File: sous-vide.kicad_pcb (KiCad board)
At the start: 2 copper layers, 100 x 70 mm, 31 parts, among them J1 Heater, J2 Power, J3 Conn_01x02, J4 Jumper, J5 Jumper, Q1 2N3904, SW1 SW_Push_Dual, SW2 SW_Push_Dual, U1 G5LE, U2 RAC01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

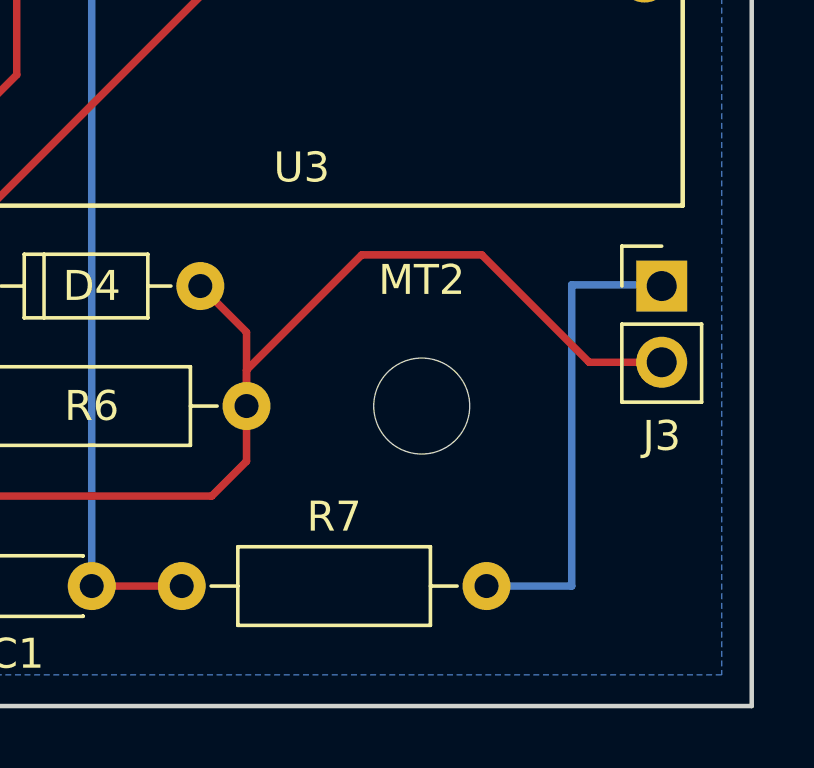
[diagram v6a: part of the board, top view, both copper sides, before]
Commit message: new schematic using NC7SB analog multiplexer
 - requires surface mount :(
 - re-annotated everything so routing will be very annoying

Also, I was testing to see why/how relay load affected analog readings
and I discovered a few odd things:

 - D4/GPIO2/Blue_LED does not light up. low voltage?
 - using a transistor on *just* the pot (instead of GPIO directly)
 seemed to remove effect of relay
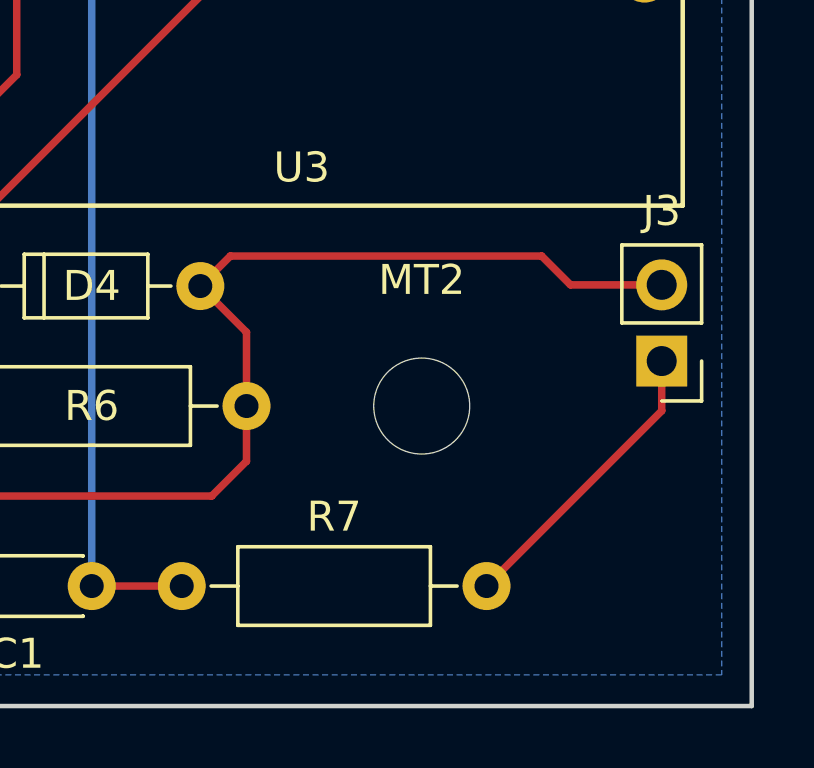
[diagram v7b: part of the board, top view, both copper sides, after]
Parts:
- moved J3 2.50 mm to (203.0, 93.5), turned to 180 degrees
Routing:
- net Net-(J3-Pad1): track 15.9 -> 9.98 mm
- net Net-(C1-Pad2): track 37.6 -> 35.7 mm
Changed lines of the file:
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@@
     (thickness 1.6)
     (drawings 95)
-    (tracks 142)
+    (tracks 139)
     (zones 0)
     (modules 31)
@@
   )
   (module Pin_Headers:Pin_Header_Straight_1x02_Pitch2.54mm (layer F.Cu)
-    (at 203 91)
+    (at 203 93.5 180)
     (descr "Through hole straight pin header, 1x02, 2.54mm pitch, single row")
     (tags "Through hole pin header THT 1x02 2.54mm single row")
-    (fp_text reference J3 (at 0 5) (layer F.SilkS)
-      (effects (font (size 1 1) (thickness 0.15)))
-    )
-    (fp_text value Conn_01x02 (at 0 4.87) (layer F.Fab)
+    (fp_text reference J3 (at 0 5 180) (layer F.SilkS)
+      (effects (font (size 1 1) (thickness 0.15)))
+    )
+    (fp_text value Conn_01x02 (at 0 4.87 180) (layer F.Fab)
       (effects (font (size 1 1) (thickness 0.15)))
     )
@@
     (fp_line (start 1.8 4.35) (end 1.8 -1.8) (layer F.CrtYd) (width 0.05))
     (fp_line (start 1.8 -1.8) (end -1.8 -1.8) (layer F.CrtYd) (width 0.05))
-    (fp_text user %R (at 0 1.27 90) (layer F.Fab)
-      (effects (font (size 1 1) (thickness 0.15)))
-    )
-    (pad 1 thru_hole rect (at 0 0) (size 1.7 1.7) (drill 1) (layers *.Cu *.Mask)
+    (fp_text user %R (at 0 1.27 270) (layer F.Fab)
+      (effects (font (size 1 1) (thickness 0.15)))
+    )
+    (pad 1 thru_hole rect (at 0 0 180) (size 1.7 1.7) (drill 1) (layers *.Cu *.Mask)
       (net 33 "Net-(J3-Pad1)"))
-    (pad 2 thru_hole oval (at 0 2.54) (size 1.7 1.7) (drill 1) (layers *.Cu *.Mask)
+    (pad 2 thru_hole oval (at 0 2.54 180) (size 1.7 1.7) (drill 1) (layers *.Cu *.Mask)
       (net 32 "Net-(C1-Pad2)"))
     (model ${KISYS3DMOD}/Pin_Headers.3dshapes/Pin_Header_Straight_1x02_Pitch2.54mm.wrl
@@
   (segment (start 121.5 39.38) (end 117.8575 39.38) (width 2.5) (layer B.Cu) (net 23))
   (segment (start 136.76 39.38) (end 121.5 39.38) (width 2.5) (layer B.Cu) (net 23))
-  (segment (start 203 93.54) (end 200.58 93.54) (width 0.25) (layer F.Cu) (net 32))
-  (segment (start 189.16 93.8) (end 189.16 95) (width 0.25) (layer F.Cu) (net 32))
-  (segment (start 193 89.96) (end 189.16 93.8) (width 0.25) (layer F.Cu) (net 32))
-  (segment (start 197 89.96) (end 193 89.96) (width 0.25) (layer F.Cu) (net 32))
-  (segment (start 200.58 93.54) (end 197 89.96) (width 0.25) (layer F.Cu) (net 32))
+  (segment (start 203 90.96) (end 199.96 90.96) (width 0.25) (layer F.Cu) (net 32))
+  (segment (start 188.62 90) (end 187.62 91) (width 0.25) (layer F.Cu) (net 32))
+  (segment (start 199 90) (end 188.62 90) (width 0.25) (layer F.Cu) (net 32))
+  (segment (start 199.96 90.96) (end 199 90) (width 0.25) (layer F.Cu) (net 32))
   (segment (start 189.16 95) (end 189.16 92.54) (width 0.25) (layer F.Cu) (net 32) (status 10))
   (segment (start 189.16 92.54) (end 187.62 91) (width 0.25) (layer F.Cu) (net 32) (status 20))
@@
   (segment (start 188 98) (end 180 98) (width 0.25) (layer F.Cu) (net 32))
   (segment (start 189.16 96.84) (end 188 98) (width 0.25) (layer F.Cu) (net 32))
-  (segment (start 200 90.96) (end 202.96 90.96) (width 0.25) (layer B.Cu) (net 33))
-  (segment (start 202.96 90.96) (end 203 91) (width 0.25) (layer B.Cu) (net 33))
-  (segment (start 197.16 101) (end 200 101) (width 0.25) (layer B.Cu) (net 33) (status 10))
-  (segment (start 200 101) (end 200 90.96) (width 0.25) (layer B.Cu) (net 33))
-  (segment (start 200 90.96) (end 200 91) (width 0.25) (layer B.Cu) (net 33))
+  (segment (start 203 93.5) (end 203 95.16) (width 0.25) (layer F.Cu) (net 33))
+  (segment (start 203 95.16) (end 197.16 101) (width 0.25) (layer F.Cu) (net 33))
+  (segment (start 202.96 93.46) (end 203 93.5) (width 0.25) (layer B.Cu) (net 33) (status 30))
   (segment (start 129.14 47) (end 136.76 54.62) (width 2.5) (layer B.Cu) (net 34) (status 10))
   (segment (start 128.5 47) (end 129.14 47) (width 2.5) (layer B.Cu) (net 34) (status 30))

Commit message: regenerated and saved everything
 - no changes to pcb
 - generated gerber files, drill file, schematic and BOM
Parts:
- R3: value 500 -> 430
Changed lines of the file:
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@@
       (effects (font (size 1 1) (thickness 0.15)))
     )
-    (fp_text value 500 (at 5.08 2.31 90) (layer F.Fab)
+    (fp_text value 430 (at 5.08 2.31 90) (layer F.Fab)
       (effects (font (size 1 1) (thickness 0.15)))
     )
